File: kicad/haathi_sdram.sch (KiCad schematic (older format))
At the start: 12 parts

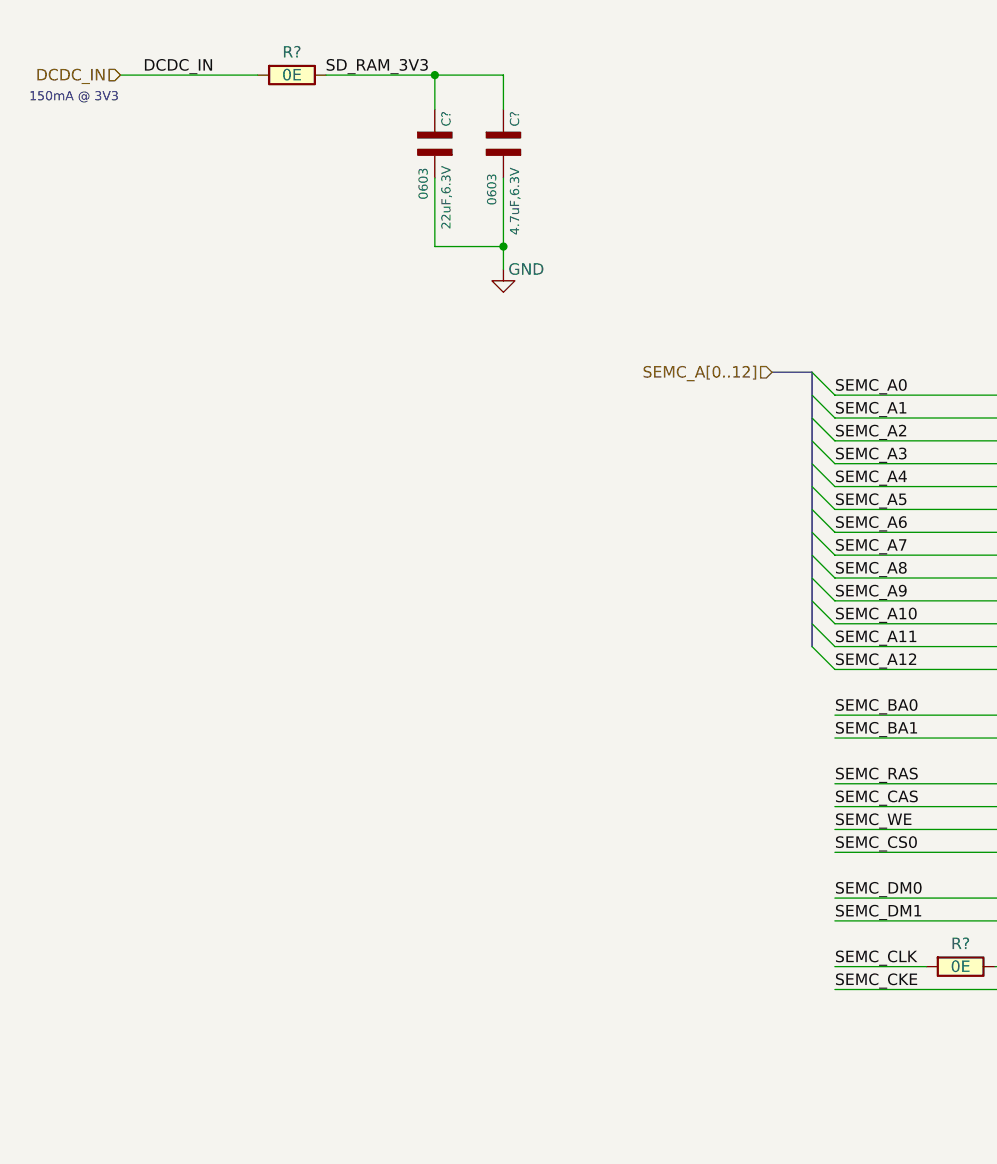
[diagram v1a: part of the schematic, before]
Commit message: Few local labels made hierarchical and VCC is now from 3V3 as opposed to DCDC_IN
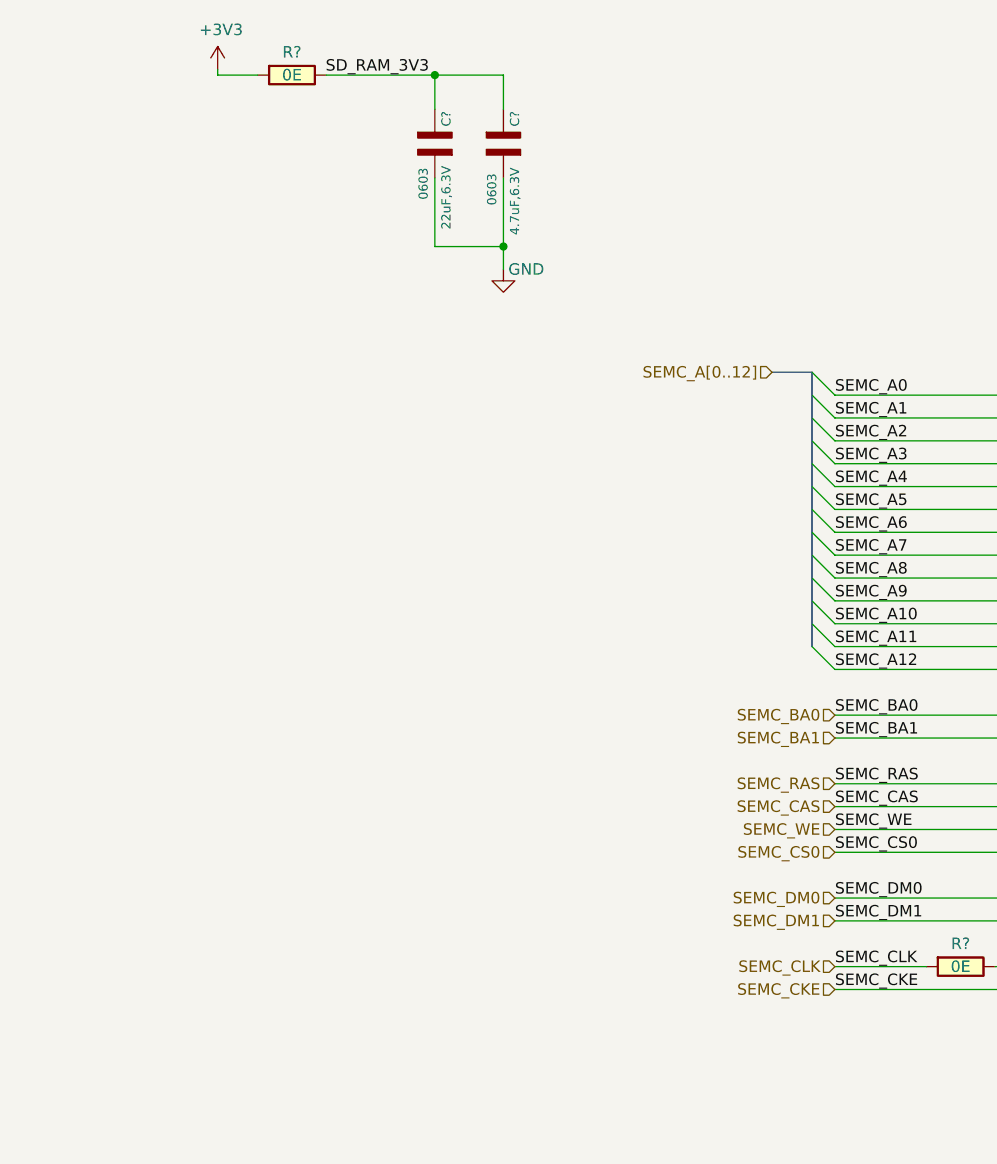
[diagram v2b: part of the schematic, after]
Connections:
- net DCDC_IN renamed +3V3
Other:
- note removed: "150mA @ 3V3"
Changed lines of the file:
@@
 EESchema Schematic File Version 4
-LIBS:haathi_schematic-cache
+LIBS:haathi_sdram-cache
 EELAYER 26 0
 EELAYER END
 $Descr A4 11693 8268
 encoding utf-8
-Sheet 9 9
+Sheet 1 1
 Title "haathi_cam"
 Date "2018-03-11"
@@
 Text Label 8000 2300 2    50   ~ 0
 SD_RAM_3V3
-Wire Wire Line
-	975  900  1575 900
-Text HLabel 975  900  0    50   Input ~ 0
-DCDC_IN
-Text Label 1075 900  0    50   ~ 0
-DCDC_IN
 $Comp
 L haathi:R R?
@@
 	1    0    0    -1
 $EndComp
-Text Notes 575  1025 0    40   ~ 0
-150mA @ 3V3
 $Comp
 L haathi:R R?
@@
 Text Notes 10075 3900 0    40   ~ 0
 One Capacitor for each\npower pin pair
+Text HLabel 4100 3700 0    50   Input ~ 0
+SEMC_BA0
+Text HLabel 4100 3800 0    50   Input ~ 0
+SEMC_BA1
+Text HLabel 4100 4000 0    50   Input ~ 0
+SEMC_RAS
+Text HLabel 4100 4100 0    50   Input ~ 0
+SEMC_CAS
+Text HLabel 4100 4200 0    50   Input ~ 0
+SEMC_WE
+Text HLabel 4100 4300 0    50   Input ~ 0
+SEMC_CS0
+Text HLabel 4100 4500 0    50   Input ~ 0
+SEMC_DM0
+Text HLabel 4100 4600 0    50   Input ~ 0
+SEMC_DM1
+Text HLabel 4100 4800 0    50   Input ~ 0
+SEMC_CLK
+Text HLabel 4100 4900 0    50   Input ~ 0
+SEMC_CKE
+$Comp
+L haathi_mayank:+3V3 #PWR?
+U 1 1 5AD204E9
+P 1400 875
+F 0 "#PWR?" H 1400 725 50  0001 C CNN
+F 1 "+3V3" H 1415 1048 50  0000 C CNN
+F 2 "" H 1400 875 50  0001 C CNN
+F 3 "" H 1400 875 50  0001 C CNN
+	1    1400 875
+	1    0    0    -1
+$EndComp
+Wire Wire Line
+	1400 875  1400 900
+Wire Wire Line
+	1400 900  1575 900
 Wire Bus Line
 	8100 3200 8100 3900

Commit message: Annotated schematic
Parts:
- gave numbers to parts that had none: 12
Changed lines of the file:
@@
 $EndDescr
 $Comp
-L haathi:MT48LC16M16A2B4 U?
+L haathi:MT48LC16M16A2B4 U7
 U 1 1 5AA58D90
 P 6000 4000
-F 0 "U?" H 6075 6025 60  0000 C CNN
+F 0 "U7" H 6075 6025 60  0000 C CNN
 F 1 "MT48LC16M16A2B4" H 6075 5925 60  0000 C CNB
 F 2 "" H 6050 4350 50  0001 C CNN
@@
 Connection ~ 5000 5700
 $Comp
-L power:GND #PWR?
+L power:GND #PWR096
 U 1 1 5AA69D4E
 P 5000 6000
-F 0 "#PWR?" H 5000 5750 50  0001 C CNN
+F 0 "#PWR096" H 5000 5750 50  0001 C CNN
 F 1 "GND" H 5050 5800 50  0000 C CNN
 F 2 "" H 5000 6000 50  0001 C CNN
@@
 SD_RAM_3V3
 $Comp
-L haathi:R R?
+L haathi:R R83
 U 1 1 5AA7F608
 P 1725 900
-F 0 "R?" V 1625 900 50  0000 C CNN
+F 0 "R83" V 1625 900 50  0000 C CNN
 F 1 "0E" V 1725 900 50  0000 C CNN
 F 2 "" V 1655 900 30  0000 C CNN
@@
 SD_RAM_3V3
 $Comp
-L haathi:C_NP C?
+L haathi:C_NP C111
 U 1 1 5AA94B59
 P 9850 3150
-F 0 "C?" V 9900 3225 40  0000 L CNN
+F 0 "C111" V 9900 3225 40  0000 L CNN
 F 1 "100nF" V 9900 2875 40  0000 L CNN
 F 2 "0603" V 9800 2975 40  0000 C CNN
@@
 	10050 3550 10250 3550
 $Comp
-L power:GND #PWR?
+L power:GND #PWR097
 U 1 1 5AAA95B6
 P 9850 3650
-F 0 "#PWR?" H 9850 3400 50  0001 C CNN
+F 0 "#PWR097" H 9850 3400 50  0001 C CNN
 F 1 "GND" H 9950 3650 50  0000 C CNN
 F 2 "" H 9850 3650 50  0001 C CNN
@@
 Connection ~ 9850 3550
 $Comp
-L haathi:C_NP C?
+L haathi:C_NP C109
 U 1 1 5AAAB501
 P 2350 1200
-F 0 "C?" V 2400 1275 40  0000 L CNN
+F 0 "C109" V 2400 1275 40  0000 L CNN
 F 1 "22uF,6.3V" V 2400 825 40  0000 L CNN
 F 2 "0603" V 2300 1025 40  0000 C CNN
@@
 $EndComp
 $Comp
-L haathi:C_NP C?
+L haathi:C_NP C110
 U 1 1 5AAAB583
 P 2650 1200
-F 0 "C?" V 2700 1275 40  0000 L CNN
+F 0 "C110" V 2700 1275 40  0000 L CNN
 F 1 "4.7uF,6.3V" V 2700 800 40  0000 L CNN
 F 2 "0603" V 2600 1000 40  0000 C CNN
@@
 	2650 1650 2650 1350
 $Comp
-L power:GND #PWR?
+L power:GND #PWR095
 U 1 1 5AAB16E5
 P 2650 1750
-F 0 "#PWR?" H 2650 1500 50  0001 C CNN
+F 0 "#PWR095" H 2650 1500 50  0001 C CNN
 F 1 "GND" H 2750 1750 50  0000 C CNN
 F 2 "" H 2650 1750 50  0001 C CNN
@@
 Connection ~ 2650 1650
 $Comp
-L haathi:C_NP C?
+L haathi:C_NP C112
 U 1 1 5AACAD8E
 P 10050 3150
-F 0 "C?" V 10100 3225 40  0000 L CNN
+F 0 "C112" V 10100 3225 40  0000 L CNN
 F 1 "100nF" V 10100 2875 40  0000 L CNN
 F 2 "0603" V 10000 2975 40  0000 C CNN
@@
 $EndComp
 $Comp
-L haathi:C_NP C?
+L haathi:C_NP C113
 U 1 1 5AACADB8
 P 10250 3150
-F 0 "C?" V 10300 3225 40  0000 L CNN
+F 0 "C113" V 10300 3225 40  0000 L CNN
 F 1 "100nF" V 10300 2875 40  0000 L CNN
 F 2 "0603" V 10200 2975 40  0000 C CNN
@@
 $EndComp
 $Comp
-L haathi:C_NP C?
+L haathi:C_NP C114
 U 1 1 5AACADE4
 P 10450 3150
-F 0 "C?" V 10500 3225 40  0000 L CNN
+F 0 "C114" V 10500 3225 40  0000 L CNN
 F 1 "100nF" V 10500 2875 40  0000 L CNN
 F 2 "0603" V 10400 2975 40  0000 C CNN
@@
 $EndComp
 $Comp
-L haathi:C_NP C?
+L haathi:C_NP C115
 U 1 1 5AACAE12
 P 10650 3150
-F 0 "C?" V 10700 3225 40  0000 L CNN
+F 0 "C115" V 10700 3225 40  0000 L CNN
 F 1 "100nF" V 10700 2875 40  0000 L CNN
 F 2 "0603" V 10600 2975 40  0000 C CNN
@@
 $EndComp
 $Comp
-L haathi:C_NP C?
+L haathi:C_NP C116
 U 1 1 5AACAE42
 P 10850 3150
-F 0 "C?" V 10900 3225 40  0000 L CNN
+F 0 "C116" V 10900 3225 40  0000 L CNN
 F 1 "100nF" V 10900 2875 40  0000 L CNN
 F 2 "0603" V 10800 2975 40  0000 C CNN
@@
 $EndComp
 $Comp
-L haathi:C_NP C?
+L haathi:C_NP C117
 U 1 1 5AACAE74
 P 11050 3150
-F 0 "C?" V 11100 3225 40  0000 L CNN
+F 0 "C117" V 11100 3225 40  0000 L CNN
 F 1 "100nF" V 11100 2875 40  0000 L CNN
 F 2 "0603" V 11000 2975 40  0000 C CNN
@@
 $EndComp
 $Comp
-L haathi:R R?
+L haathi:R R84
 U 1 1 5AACF89B
 P 4650 4800
-F 0 "R?" V 4550 4800 50  0000 C CNN
+F 0 "R84" V 4550 4800 50  0000 C CNN
 F 1 "0E" V 4650 4800 50  0000 C CNN
 F 2 "" V 4580 4800 30  0000 C CNN
@@
 SEMC_CKE
 $Comp
-L haathi_mayank:+3V3 #PWR?
+L haathi_mayank:+3V3 #PWR094
 U 1 1 5AD204E9
 P 1400 875
-F 0 "#PWR?" H 1400 725 50  0001 C CNN
+F 0 "#PWR094" H 1400 725 50  0001 C CNN
 F 1 "+3V3" H 1415 1048 50  0000 C CNN
 F 2 "" H 1400 875 50  0001 C CNN

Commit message: ERC pass 1: Check and resolve the errors
Signed-off-by: Kumar Abhishek <abhishek@theembeddedkitchen.net>
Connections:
- wire segments 92 -> 93
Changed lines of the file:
@@
 EESchema Schematic File Version 4
-LIBS:haathi_schematic-cache
+LIBS:haathi-cache
 EELAYER 26 0
 EELAYER END
 $Descr A4 11693 8268
 encoding utf-8
-Sheet 7 9
+Sheet 7 11
 Title "haathi_cam"
 Date "2018-03-11"
@@
 Wire Wire Line
 	1400 900  1575 900
+$Comp
+L power:PWR_FLAG #FLG0101
+U 1 1 5B25E04F
+P 2650 850
+F 0 "#FLG0101" H 2650 925 50  0001 C CNN
+F 1 "PWR_FLAG" H 2650 1024 50  0000 C CNN
+F 2 "" H 2650 850 50  0001 C CNN
+F 3 "~" H 2650 850 50  0001 C CNN
+	1    2650 850
+	1    0    0    -1
+$EndComp
+Wire Wire Line
+	2650 850  2650 900
+Connection ~ 2650 900
 Wire Bus Line
 	8100 3200 8100 3900
